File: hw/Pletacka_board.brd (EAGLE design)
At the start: 160 x 100 mm, 29 parts, among them U1 LM75BDP

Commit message: Start routing
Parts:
- moved S2 47.7 mm to (59.7, 30.5), turned to 270 degrees
- moved S1 34.2 mm to (59.7, 66.0), turned to 270 degrees
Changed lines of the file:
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@@
 <attribute name="VALUE" x="34.925" y="46.355" size="1.27" layer="27"/>
 </element>
-<element name="S1" library="switch-omron" library_urn="urn:adsk.eagle:library:377" package="B3F-10XX" package3d_urn="urn:adsk.eagle:package:27496/1" value="" x="27.94" y="53.34" smashed="yes">
-<attribute name="MF" value="" x="27.94" y="53.34" size="1.778" layer="27" display="off"/>
-<attribute name="MPN" value="B3F-1000" x="27.94" y="53.34" size="1.778" layer="27" display="off"/>
-<attribute name="NAME" x="24.892" y="57.023" size="1.27" layer="25" ratio="10"/>
-<attribute name="OC_FARNELL" value="176432" x="27.94" y="53.34" size="1.778" layer="27" display="off"/>
-<attribute name="OC_NEWARK" value="36M3542" x="27.94" y="53.34" size="1.778" layer="27" display="off"/>
-<attribute name="POPULARITY" value="72" x="27.94" y="53.34" size="1.778" layer="27" display="off"/>
-<attribute name="VALUE" x="24.892" y="48.26" size="1.27" layer="27" ratio="10"/>
-</element>
-<element name="S2" library="switch-omron" library_urn="urn:adsk.eagle:library:377" package="B3F-10XX" package3d_urn="urn:adsk.eagle:package:27496/1" value="" x="17.78" y="53.34" smashed="yes">
-<attribute name="MF" value="" x="17.78" y="53.34" size="1.778" layer="27" display="off"/>
-<attribute name="MPN" value="B3F-1000" x="17.78" y="53.34" size="1.778" layer="27" display="off"/>
-<attribute name="NAME" x="14.732" y="57.023" size="1.27" layer="25" ratio="10"/>
-<attribute name="OC_FARNELL" value="176432" x="17.78" y="53.34" size="1.778" layer="27" display="off"/>
-<attribute name="OC_NEWARK" value="36M3542" x="17.78" y="53.34" size="1.778" layer="27" display="off"/>
-<attribute name="POPULARITY" value="72" x="17.78" y="53.34" size="1.778" layer="27" display="off"/>
-<attribute name="VALUE" x="14.732" y="48.26" size="1.27" layer="27" ratio="10"/>
+<element name="S1" library="switch-omron" library_urn="urn:adsk.eagle:library:377" package="B3F-10XX" package3d_urn="urn:adsk.eagle:package:27496/1" value="" x="59.69" y="66.04" smashed="yes" rot="R270">
+<attribute name="MF" value="" x="59.69" y="66.04" size="1.778" layer="27" rot="R270" display="off"/>
+<attribute name="MPN" value="B3F-1000" x="59.69" y="66.04" size="1.778" layer="27" rot="R270" display="off"/>
+<attribute name="NAME" x="63.373" y="69.088" size="1.27" layer="25" ratio="10" rot="R270"/>
+<attribute name="OC_FARNELL" value="176432" x="59.69" y="66.04" size="1.778" layer="27" rot="R270" display="off"/>
+<attribute name="OC_NEWARK" value="36M3542" x="59.69" y="66.04" size="1.778" layer="27" rot="R270" display="off"/>
+<attribute name="POPULARITY" value="72" x="59.69" y="66.04" size="1.778" layer="27" rot="R270" display="off"/>
+<attribute name="VALUE" x="54.61" y="69.088" size="1.27" layer="27" ratio="10" rot="R270"/>
+</element>
+<element name="S2" library="switch-omron" library_urn="urn:adsk.eagle:library:377" package="B3F-10XX" package3d_urn="urn:adsk.eagle:package:27496/1" value="" x="59.69" y="30.48" smashed="yes" rot="R270">
+<attribute name="MF" value="" x="59.69" y="30.48" size="1.778" layer="27" rot="R270" display="off"/>
+<attribute name="MPN" value="B3F-1000" x="59.69" y="30.48" size="1.778" layer="27" rot="R270" display="off"/>
+<attribute name="NAME" x="63.373" y="33.528" size="1.27" layer="25" ratio="10" rot="R270"/>
+<attribute name="OC_FARNELL" value="176432" x="59.69" y="30.48" size="1.778" layer="27" rot="R270" display="off"/>
+<attribute name="OC_NEWARK" value="36M3542" x="59.69" y="30.48" size="1.778" layer="27" rot="R270" display="off"/>
+<attribute name="POPULARITY" value="72" x="59.69" y="30.48" size="1.778" layer="27" rot="R270" display="off"/>
+<attribute name="VALUE" x="54.61" y="33.528" size="1.27" layer="27" ratio="10" rot="R270"/>
 </element>
 <element name="OK1" library="#Optocleny" package="DIL04" value="PC817" x="121.92" y="24.13" smashed="yes" rot="R90">
@@
 <wire x1="39.37" y1="83.3" x2="44.45" y2="83.3" width="0" layer="19" extent="1-1"/>
 <wire x1="34.29" y1="83.3" x2="39.37" y2="83.3" width="0" layer="19" extent="1-1"/>
-<wire x1="31.1912" y1="55.6006" x2="34.29" y2="83.3" width="0" layer="19" extent="1-1"/>
-<wire x1="24.6888" y1="55.6006" x2="31.1912" y2="55.6006" width="0" layer="19" extent="1-1"/>
-<wire x1="21.0312" y1="55.6006" x2="24.6888" y2="55.6006" width="0" layer="19" extent="1-1"/>
-<wire x1="14.5288" y1="55.6006" x2="21.0312" y2="55.6006" width="0" layer="19" extent="1-1"/>
-<wire x1="118.11" y1="25.4" x2="14.5288" y2="55.6006" width="0" layer="19" extent="1-1"/>
+<wire x1="61.9506" y1="62.7888" x2="34.29" y2="83.3" width="0" layer="19" extent="1-1"/>
+<wire x1="61.9506" y1="69.2912" x2="61.9506" y2="62.7888" width="0" layer="19" extent="1-1"/>
+<wire x1="61.9506" y1="27.2288" x2="61.9506" y2="69.2912" width="0" layer="19" extent="1-1"/>
+<wire x1="61.9506" y1="33.7312" x2="61.9506" y2="27.2288" width="0" layer="19" extent="1-1"/>
+<wire x1="118.11" y1="25.4" x2="61.9506" y2="33.7312" width="0" layer="19" extent="1-1"/>
 <wire x1="99.06" y1="27.94" x2="118.11" y2="25.4" width="0" layer="19" extent="1-1"/>
 <wire x1="78.74" y1="27.94" x2="99.06" y2="27.94" width="0" layer="19" extent="1-1"/>
 <wire x1="57.15" y1="27.94" x2="78.74" y2="27.94" width="0" layer="19" extent="1-1"/>
+<via x="99.06" y="27.94" extent="1-16" drill="0.35"/>
 </signal>
 <signal name="+3V3">
@@
 <contactref element="S1" pad="3"/>
 <contactref element="S1" pad="4"/>
-<wire x1="31.1912" y1="51.0794" x2="24.6888" y2="51.0794" width="0" layer="19" extent="1-1"/>
-<wire x1="36.28" y1="52.07" x2="31.1912" y2="51.0794" width="0" layer="19" extent="1-1"/>
+<wire x1="57.4294" y1="62.7888" x2="57.4294" y2="69.2912" width="0" layer="19" extent="1-1"/>
+<wire x1="36.28" y1="52.07" x2="57.4294" y2="62.7888" width="0" layer="19" extent="1-1"/>
 </signal>
 <signal name="N$10">
@@
 <contactref element="R5" pad="2"/>
 <contactref element="S2" pad="4"/>
-<wire x1="21.0312" y1="51.0794" x2="14.5288" y2="51.0794" width="0" layer="19" extent="1-1"/>
-<wire x1="36.28" y1="48.26" x2="21.0312" y2="51.0794" width="0" layer="19" extent="1-1"/>
+<wire x1="57.4294" y1="27.2288" x2="57.4294" y2="33.7312" width="0" layer="19" extent="1-1"/>
+<wire x1="36.28" y1="48.26" x2="57.4294" y2="27.2288" width="0" layer="19" extent="1-1"/>
 </signal>
 <signal name="BUTTON1">

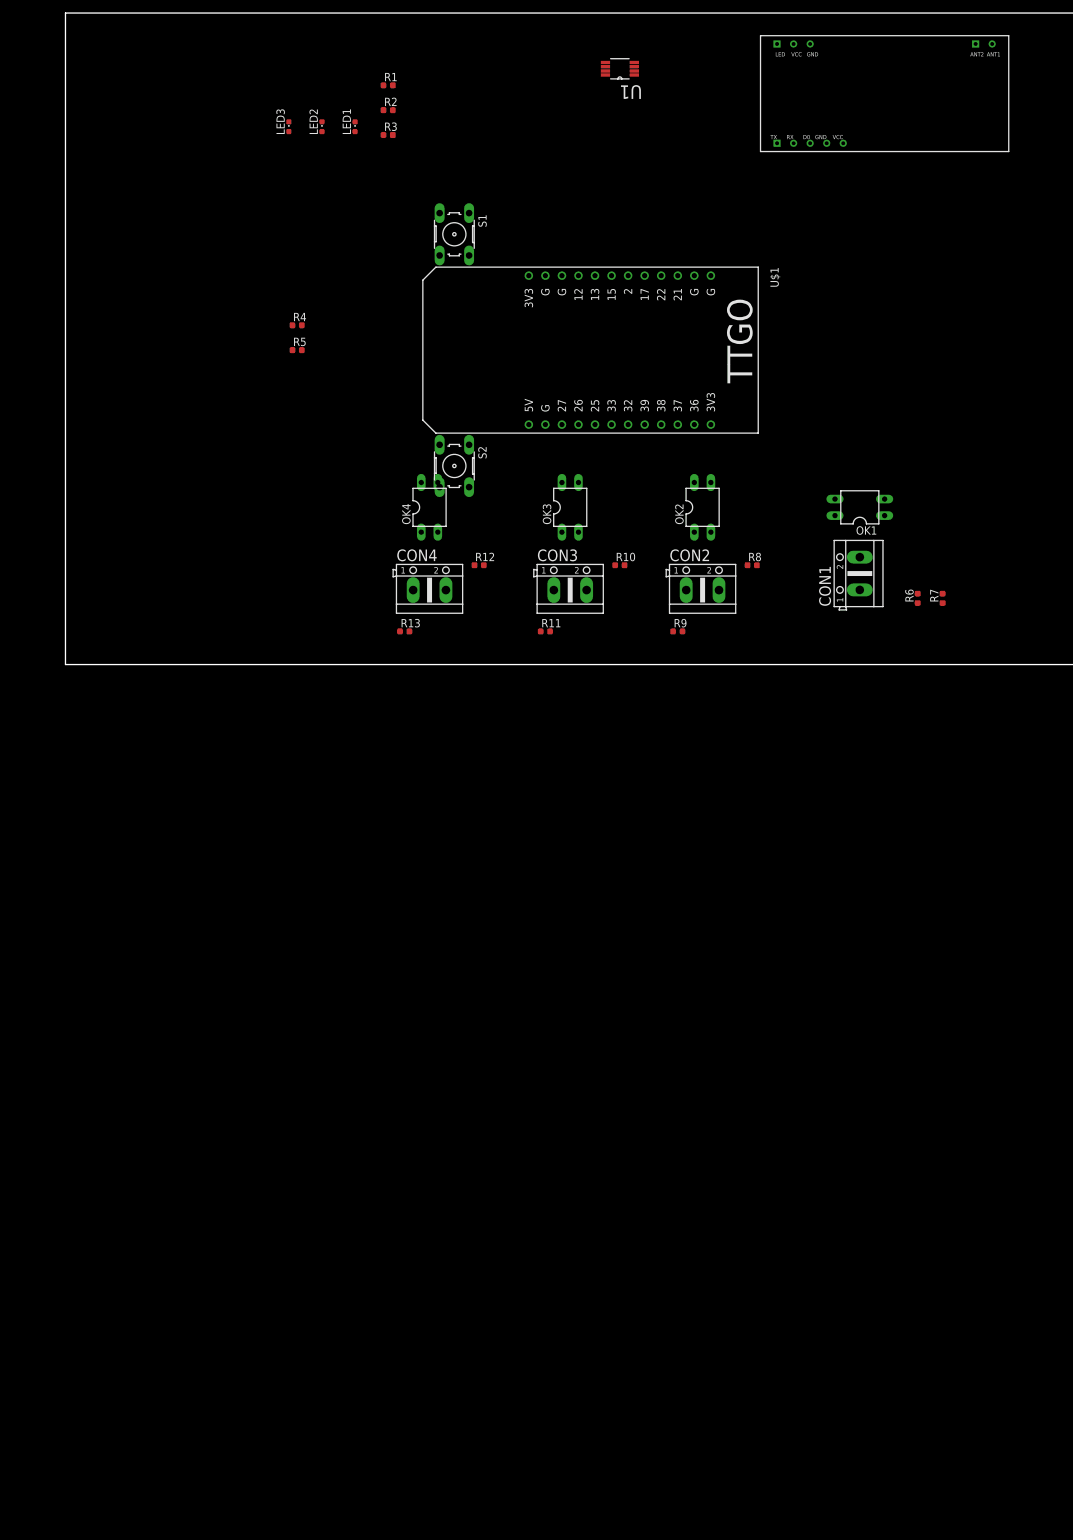
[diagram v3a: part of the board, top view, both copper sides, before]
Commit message: Start power management
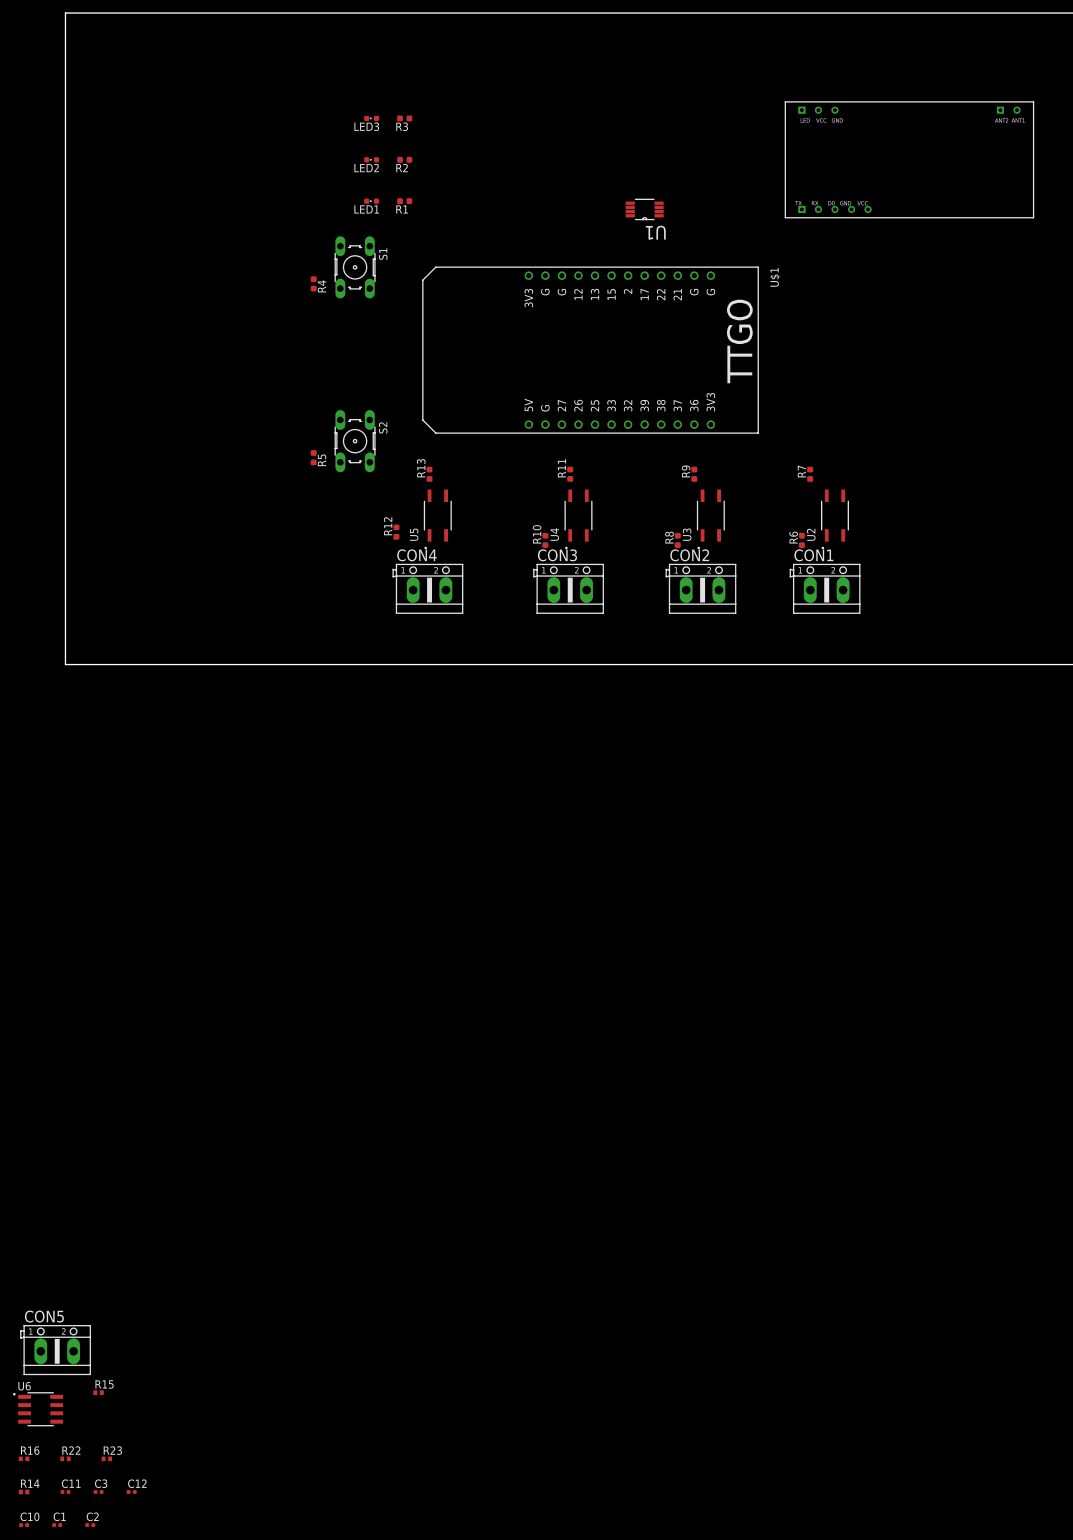
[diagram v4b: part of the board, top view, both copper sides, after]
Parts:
- removed OK1, OK2, OK3, OK4: PC817, #Optocleny:DIL04
- added C1: 10u, rcl_upravena:C0402
- added C10: 22u, rcl_upravena:C0402
- added C11: 100n, rcl_upravena:C0402
- added C12: 8.2n, rcl_upravena:C0402
- added C2: 10p, rcl_upravena:C0402
- added C3: 6.8n, rcl_upravena:C0402
- added CON5: (no value), #Svorkovnice:AK500/2
- added R14: 169K, rcl:R0402
- added R15: 16.2k, rcl:R0402
- added R16: 8.25k, rcl:R0402
- added R22: 1.69k, rcl:R0402
- added R23: 10.2k, rcl:R0402
- added U2, U3, U4, U5: EL357N(A)(TA)-G, EL357N_A__TA_-G:SOP254P700X200-4N
- added U6: TPS54231D, TPS54231D:SOIC127P599X175-8N
- moved R7 27.9 mm to (114.3, 29.2)
- moved R11 24.4 mm to (77.5, 29.2), turned to 90 degrees
- moved R13 24.4 mm to (55.9, 29.2), turned to 90 degrees
- moved R9 24.3 mm to (96.5, 29.2), turned to 90 degrees
- moved U1 21.9 mm to (88.9, 69.8)
- moved R6 19.9 mm to (113.0, 19.1)
- moved R1 18.0 mm to (52.1, 71.1), turned to 180 degrees
- moved R5 16.7 mm to (38.1, 31.8), turned to 270 degrees
- moved S1 16.1 mm to (44.5, 61.0)
- moved S2 15.7 mm to (44.5, 34.3)
- moved R12 13.7 mm to (50.8, 20.3), turned to 90 degrees
- moved LED3 12.8 mm to (47.0, 83.8), turned to 90 degrees
- moved R10 12.0 mm to (73.7, 19.1), turned to 90 degrees
- moved R8 12.0 mm to (94.0, 19.1), turned to 90 degrees
- moved LED1 11.7 mm to (47.0, 71.1), turned to 90 degrees
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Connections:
- new net N$22: C1.1, CON5.1, R14.2, U6.2
- new net N$23: R14.1, R15.2, U6.3
- new net N$25: C3.1, R16.1
- new net N$26: C2.1, R16.2, U6.6
- new net N$34: R22.2, R23.1, U6.5
- new net N$35: C11.1, U6.1
- new net N$36: C11.2, U6.8
- new net N$37: C12.1, U6.4
- net +5V: now also C10.1, R23.2
- net GND: now also C1.2, C10.2, C12.2, C2.2, C3.2, CON5.2, R15.1, R22.1, U2.3, U3.3, U4.3, U5.3, U6.7; no longer OK1.3, OK2.3, OK3.3, OK4.3
- net N$14: now also U3.2; no longer OK2.2
- net N$15: now also U3.1; no longer OK2.1
- net N$17: now also U4.2; no longer OK3.2
- net N$18: now also U4.1; no longer OK3.1
- net N$20: now also U5.2; no longer OK4.2
- net N$21: now also U5.1; no longer OK4.1
- net N$7: now also U2.2; no longer OK1.2
- net N$9: now also U2.1; no longer OK1.1
- net OPTO1: now also U2.4; no longer OK1.4
- net OPTO2: now also U3.4; no longer OK2.4
- net OPTO3: now also U4.4; no longer OK3.4
- net OPTO4: now also U5.4; no longer OK4.4

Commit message: cesgaw
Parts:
- added C4, C5: 1u, rcl_upravena:C0603
- added D1: B5819W, B5819W:SOD-123
- R1, R2, R3, R4, R5: value 330R -> 2k2
- R11, R13, R7, R9: value (none) -> 10k
- R14: value 169K -> 160k
- R15: value 16.2k -> 16k
- R16: value 8.25k -> 8.2k
- R22: value 1.69k -> 1.8k
- R23: value 10.2k -> 10k
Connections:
- net GND: now also C4.1, C5.1, D1.A
- net N$10: now also C4.2
- net N$36: now also D1.C
- net N$8: now also C5.2

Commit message: Start routing
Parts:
- removed RDM1: RDM6300, RDM6300:RDM6300
- added U$2: SWRB1204S, SWRB1204S-680MT:SWRB1204S
- C1, C10, C11, C12, C2, C3: device rcl_upravena:C0402 -> rcl_upravena:C0603
- R10, R12, R6, R8: value (none) -> 1k
- R14, R15, R16, R22, R23: device rcl:R0402 -> rcl_upravena:R0603
- S1, S2: value (none) -> CHOOSE_ME; device switch-omron:B3F-10XX -> switch-omron:TS-1187A
- moved C5 203.2 mm to (-9.53, 54.6), turned to 270 degrees
- moved C4 181.6 mm to (-6.35, 36.8), turned to 270 degrees
- moved D1 175.2 mm to (60.3, 24.1), turned to 180 degrees
- moved C10 174.0 mm to (59.1, 29.2), turned to 180 degrees
- moved C1 161.7 mm to (52.7, 20.3), turned to 90 degrees
- moved C2 160.4 mm to (64.1, 16.5), turned to 90 degrees
- moved C11 159.9 mm to (62.2, 20.3)
- moved C3 156.2 mm to (66.7, 16.5), turned to 90 degrees
- moved R14 154.9 mm to (52.1, 16.5), turned to 90 degrees
- moved R22 154.8 mm to (69.2, 16.5), turned to 270 degrees
- moved R16 152.5 mm to (65.4, 12.7), turned to 180 degrees
- moved C12 147.6 mm to (54.0, 14.0), turned to 270 degrees
- moved R23 146.8 mm to (70.5, 10.2)
- moved U6 145.1 mm to (59.1, 16.5)
- moved R15 133.0 mm to (52.1, 12.7), turned to 90 degrees
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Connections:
- net N$22 renamed VIN
- net N$23 renamed EN
- net N$26 renamed COMP
- net N$34 renamed VSENSE
- net N$35 renamed BOOT
- net N$37 renamed SS
- removed net N$11: U$1.33
- removed net N$36: C11.2, D1.C, U6.8
- new net PH: C11.2, D1.C, U$2.P$1, U6.8
- new net TMP_OS: U$1.33, U1.3
- net +5V: now also U$2.P$2; no longer RDM1.VCC
- net GND: now also S1.A, S1.B, S2.A, S2.B, U1.5, U1.6, U1.7; no longer RDM1.GND, S1.1, S1.2, S2.1, S2.2
- net N$10: now also S2.C, S2.D; no longer S2.3, S2.4
- net N$8: now also S1.C, S1.D; no longer S1.3, S1.4
- net RFID: no longer RDM1.RX
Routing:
- net GND: track 0.00 -> 42.7 mm
- net +5V: track 0.00 -> 37.9 mm
- net VIN: track 0.00 -> 24.9 mm
- net PH: track 0.00 -> 18.2 mm
- net VSENSE: track 0.00 -> 17.8 mm
- net EN: track 0.00 -> 6.92 mm
- net COMP: track 0.00 -> 6.38 mm
- net N$25: track 0.00 -> 3.32 mm
- net SS: track 0.00 -> 2.65 mm
- added copper zone on layer 1, net GND
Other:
- board size 160 x 100 mm -> 74.9 x 100 mm
